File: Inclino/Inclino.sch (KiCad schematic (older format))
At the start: 44 parts

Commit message: Add DAC Digital
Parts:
- Q?: value Q_NMOS_DSG -> PMV65UN
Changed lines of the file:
@@
 P 14600 6800
 F 0 "Q?" H 14800 6850 50  0000 L CNN
-F 1 "Q_NMOS_DSG" H 14800 6750 50  0000 L CNN
+F 1 "PMV65UN" H 14800 6750 50  0000 L CNN
 F 2 "" H 14800 6900 50  0001 C CNN
 F 3 "" H 14600 6800 50  0001 C CNN

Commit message: Set Inclino footprint
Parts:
- removed C? (x2): C, symbol C
- removed Q?: PMV65UN, symbol Q_NMOS_DSG
- removed SW? (x4): SW_DIP_x01, symbol SW_DIP_x01
- added C6, C7: 100n, Yame_library:SM0603-MR, symbol C
- added Q1: PMV65UN, Yame_library:SOT23-MR, symbol N-MOS_SOT23
- added SW1, SW2, SW3, SW4: SW_Push, Buttons_Switches_SMD:SW_SPST_FSMSM, symbol SW_Push
- BT1, BT2: renamed from BT?; value Battery_Cell -> Keystone_2466; footprint (none) -> Yame_library:AAA_2466
- C10: renamed from C?; footprint (none) -> Capacitors_Tantalum_SMD:CP_Tantalum_Case-B_EIA-3528-21_Hand
- C11, C12: renamed from C?; footprint (none) -> Yame_library:SM0603-MR
- C13: renamed from C?; footprint (none) -> Yame_library:SM0805-MR
- C5: renamed from C?; value C -> 100n; footprint (none) -> Yame_library:SM0603-MR
- L1: renamed from L?; footprint (none) -> Yame_library:MLC15xx
- R1, R10, R11, R12, R2, R3, R4, R5, R6, R7, R8, R9: renamed from R?; footprint (none) -> Yame_library:SM0603-MR
- U1: renamed from U?; footprint (none) -> Housings_SOIC:SOIC-24W_7.5x15.4mm_Pitch1.27mm
- U10: renamed from U?; footprint (none) -> Housings_SSOP:HTSSOP-16-1EP_4.4x5mm_Pitch0.65mm_ThermalVias
- U2: renamed from U?; footprint (none) -> Housings_DIP:SMDIP-12_W11.48mm
- U3, U4, U5, U6, U8, U9: renamed from U?; footprint (none) -> Displays_7-Segment:7SegmentLED_LTS6760_LTS6780
- U7: renamed from U?; footprint (none) -> Housings_SOIC:SOIC-14_3.9x8.7mm_Pitch1.27mm
- gave numbers to parts that had none: 7
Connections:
- wire segments 201 -> 202
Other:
- moved on the sheet: R12

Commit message: Set footprints
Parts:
- P1: symbol CONN_01X05 -> Conn_01x05
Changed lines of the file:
@@
 EESchema Schematic File Version 2
+LIBS:Inclino-rescue
 LIBS:power
 LIBS:device
@@
 LIBS:valves
 LIBS:YameLib
-LIBS:Inclino-cache
 EELAYER 25 0
 EELAYER END
@@
 $EndDescr
 $Comp
-L CONN_01X05 P1
+L Conn_01x05 P1
 U 1 1 59D25512
 P 6100 6550

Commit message: Send Inclino PCB
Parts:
- removed R8: 100k, Yame_library:SM0603-MR, symbol R
- added J1, J2: Fix, Mounting_Holes:MountingHole_3.2mm_M3, symbol Conn_01x01
- added J3, J4, J5, J6: Conn_01x03, Yame_library:Inc_90°, symbol Conn_01x03
- SW4: value SW_Push -> SW_Power
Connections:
- net labels added: +5v_R, +Vsw, /CS_INC_R, BATT_LowSide, GND_R, MISO_R, MOSI_R, SCK_R
- wire segments 202 -> 222
- no-connect marks 0 -> 2
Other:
- moved on the sheet: C1, C2, Q1, R12, SW4, U2

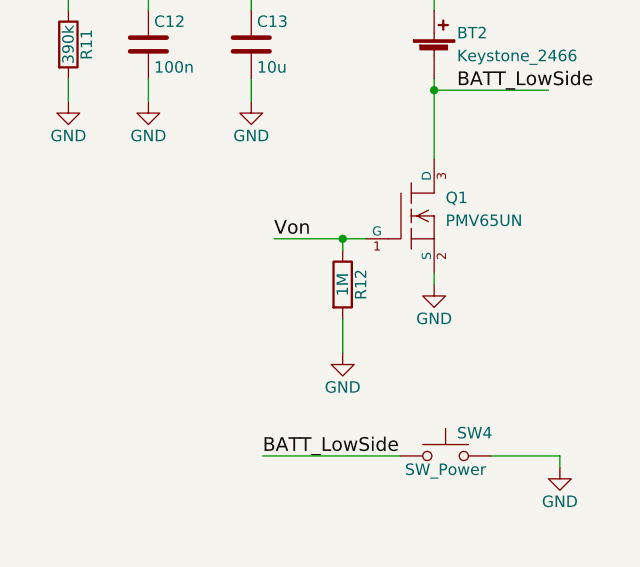
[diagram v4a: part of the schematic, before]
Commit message: Fix Inclino bug
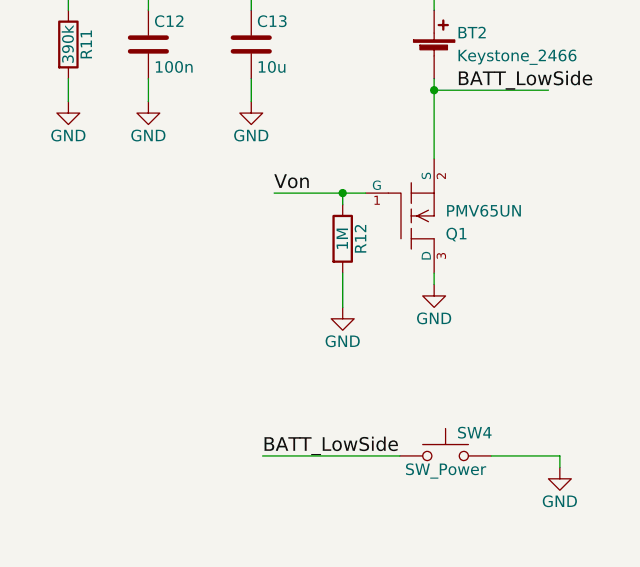
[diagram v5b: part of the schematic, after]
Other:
- moved on the sheet: R12
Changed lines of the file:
@@
 L R R12
 U 1 1 59D357A8
-P 14100 7350
-F 0 "R12" V 14180 7350 50  0000 C CNN
-F 1 "1M" V 14100 7350 50  0000 C CNN
-F 2 "Yame_library:SM0603-MR" V 14030 7350 50  0001 C CNN
-F 3 "" H 14100 7350 50  0001 C CNN
-	1    14100 7350
-	1    0    0    -1
-$EndComp
-Text Label 13800 7150 0    60   ~ 0
+P 14100 7150
+F 0 "R12" V 14180 7150 50  0000 C CNN
+F 1 "1M" V 14100 7150 50  0000 C CNN
+F 2 "Yame_library:SM0603-MR" V 14030 7150 50  0001 C CNN
+F 3 "" H 14100 7150 50  0001 C CNN
+	1    14100 7150
+	1    0    0    -1
+$EndComp
+Text Label 13800 6950 0    60   ~ 0
 Von
 Text Label 8500 7250 0    60   ~ 0
@@
 Connection ~ 14500 6500
 Wire Wire Line
-	13800 7150 14200 7150
+	13800 6950 14200 6950
 Wire Wire Line
 	13750 8100 14350 8100
@@
 F 3 "" H 14400 7050 60  0000 C CNN
 	1    14400 7050
-	1    0    0    -1
-$EndComp
-Wire Wire Line
-	14100 7500 14100 7650
+	1    0    0    1
+$EndComp
+Wire Wire Line
+	14100 7300 14100 7450
 $Comp
 L Conn_01x01 J1
@@
 L GND #PWR025
 U 1 1 59F468E8
-P 14100 7650
-F 0 "#PWR025" H 14100 7400 50  0001 C CNN
-F 1 "GND" H 14100 7500 50  0000 C CNN
-F 2 "" H 14100 7650 60  0000 C CNN
-F 3 "" H 14100 7650 60  0000 C CNN
-	1    14100 7650
-	1    0    0    -1
-$EndComp
-Wire Wire Line
-	14100 7200 14100 7150
-Connection ~ 14100 7150
+P 14100 7450
+F 0 "#PWR025" H 14100 7200 50  0001 C CNN
+F 1 "GND" H 14100 7300 50  0000 C CNN
+F 2 "" H 14100 7450 60  0000 C CNN
+F 3 "" H 14100 7450 60  0000 C CNN
+	1    14100 7450
+	1    0    0    -1
+$EndComp
+Wire Wire Line
+	14100 7000 14100 6950
+Connection ~ 14100 6950
 Wire Wire Line
 	14500 6500 15000 6500
